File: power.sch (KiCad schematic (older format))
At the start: 20 parts, among them J4 DYN, J7 LI+, U3 LF50_TO220, U4 MCP73832-2-OT, U5 TLV75733PDBV, U6 TS881xLx

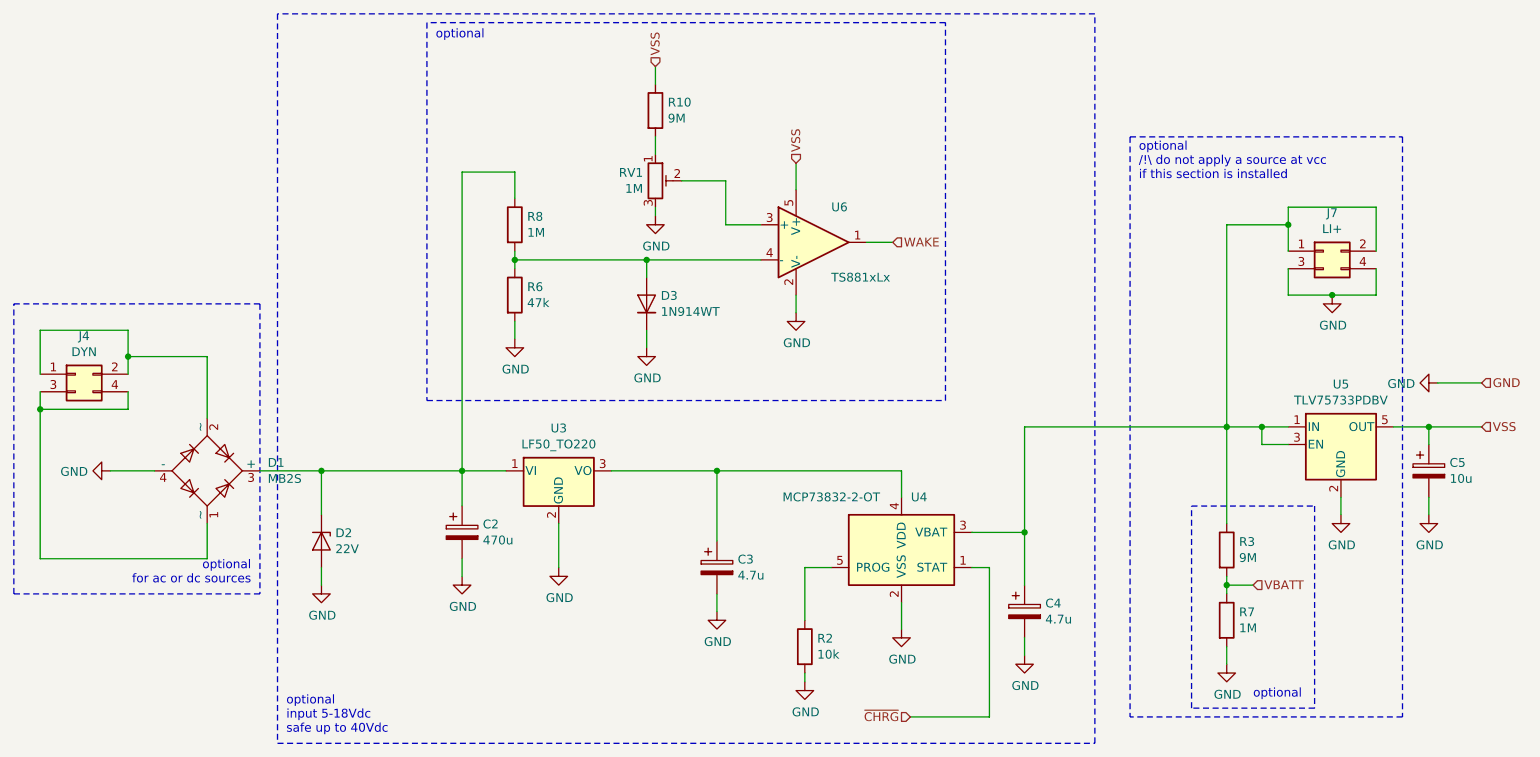
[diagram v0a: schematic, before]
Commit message: added readme and specified some field values
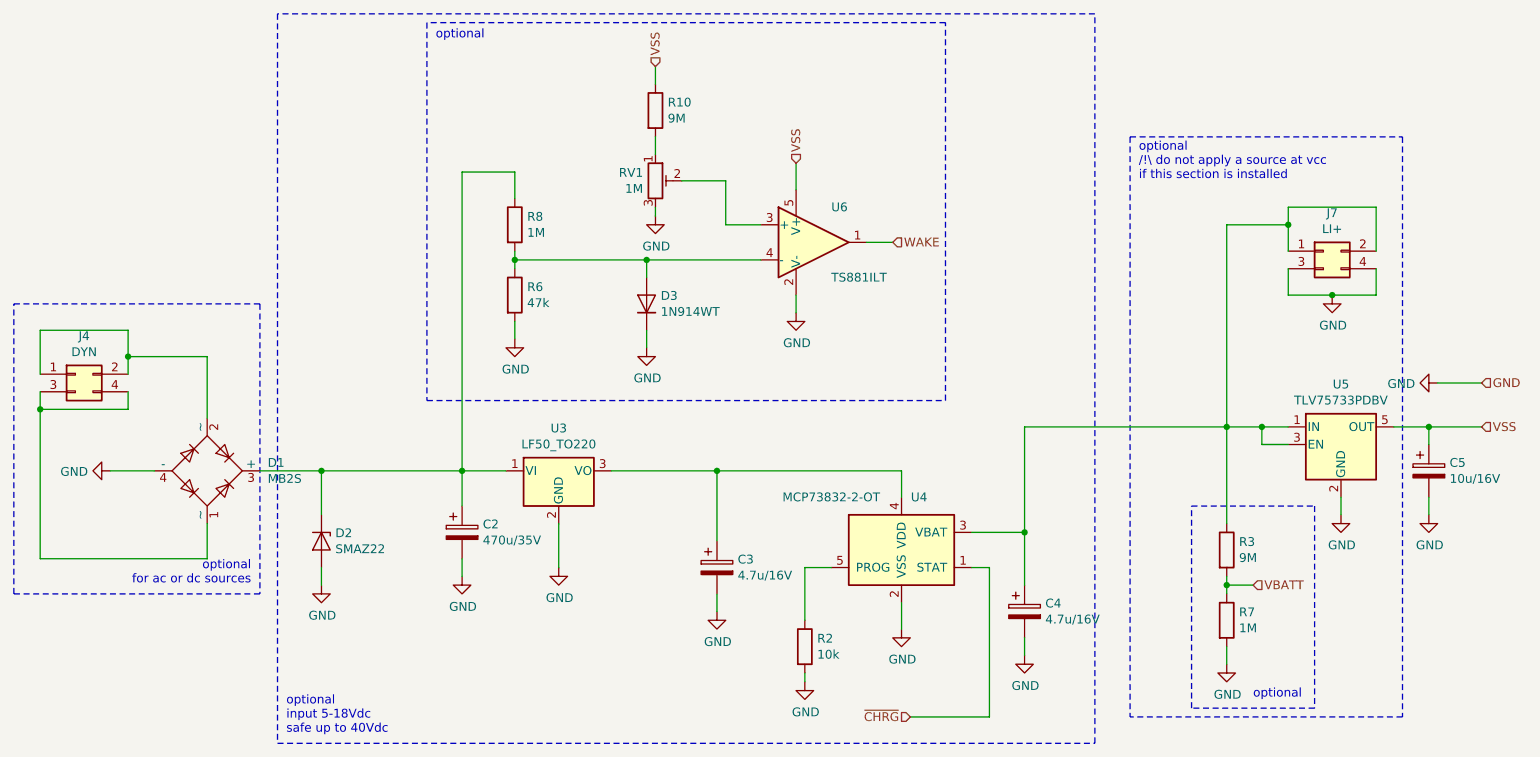
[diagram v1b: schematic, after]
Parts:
- C2: value 470u -> 470u/35V
- C3, C4: value 4.7u -> 4.7u/16V
- C5: value 10u -> 10u/16V
- D2: value 22V -> SMAZ22
- U6: value TS881xLx -> TS881ILT
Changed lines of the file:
@@
 P 6200 3050
 F 0 "U6" H 6300 3250 50  0000 L CNN
-F 1 "TS881xLx" H 6300 2850 50  0000 L CNN
+F 1 "TS881ILT" H 6300 2850 50  0000 L CNN
 F 2 "Package_TO_SOT_SMD:SOT-23-5" H 6100 2850 50  0001 L CNN
 F 3 "www.st.com/resource/en/datasheet/ts881.pdf" H 6200 3250 50  0001 C CNN
@@
 P 9700 4350
 F 0 "C5" H 9818 4396 50  0000 L CNN
-F 1 "10u" H 9818 4305 50  0000 L CNN
+F 1 "10u/16V" H 9818 4305 50  0000 L CNN
 F 2 "Capacitor_Tantalum_SMD:CP_EIA-6032-28_Kemet-C_Pad2.25x2.35mm_HandSolder" H 9738 4200 50  0001 C CNN
-F 3 "~" H 9700 4350 50  0001 C CNN
+F 3 "https://www.mouser.de/datasheet/2/212/KEM_T2005_T491-1093550.pdf" H 9700 4350 50  0001 C CNN
 	1    9700 4350
 	1    0    0    -1
@@
 P 4200 4700
 F 0 "C2" H 4318 4746 50  0000 L CNN
-F 1 "470u" H 4318 4655 50  0000 L CNN
+F 1 "470u/35V" H 4318 4655 50  0000 L CNN
 F 2 "Capacitor_THT:CP_Radial_D8.0mm_P3.50mm" H 4238 4550 50  0001 C CNN
 F 3 "https://www.mouser.de/datasheet/2/315/ABA0000C1022-1144690.pdf" H 4200 4700 50  0001 C CNN
@@
 P 7400 5150
 F 0 "C4" H 7518 5196 50  0000 L CNN
-F 1 "4.7u" H 7518 5105 50  0000 L CNN
+F 1 "4.7u/16V" H 7518 5105 50  0000 L CNN
 F 2 "Capacitor_Tantalum_SMD:CP_EIA-6032-28_Kemet-C_Pad2.25x2.35mm_HandSolder" H 7650 4150 50  0001 C CNN
-F 3 "~" H 7400 5150 50  0001 C CNN
+F 3 "https://www.mouser.de/datasheet/2/212/KEM_T2005_T491-1093550.pdf" H 7400 5150 50  0001 C CNN
 	1    7400 5150
 	1    0    0    -1
@@
 P 5650 4900
 F 0 "C3" H 5768 4946 50  0000 L CNN
-F 1 "4.7u" H 5768 4855 50  0000 L CNN
+F 1 "4.7u/16V" H 5768 4855 50  0000 L CNN
 F 2 "Capacitor_Tantalum_SMD:CP_EIA-6032-28_Kemet-C_Pad2.25x2.35mm_HandSolder" H 5688 4750 50  0001 C CNN
-F 3 "~" H 5650 4900 50  0001 C CNN
+F 3 "https://www.mouser.de/datasheet/2/212/KEM_T2005_T491-1093550.pdf" H 5650 4900 50  0001 C CNN
 	1    5650 4900
 	1    0    0    -1
@@
 P 3400 4750
 F 0 "D2" V 3354 4829 50  0000 L CNN
-F 1 "22V" V 3445 4829 50  0000 L CNN
+F 1 "SMAZ22" V 3445 4829 50  0000 L CNN
 F 2 "Diode_SMD:D_SMA_Handsoldering" H 3400 4750 50  0001 C CNN
 F 3 "https://www.mouser.de/datasheet/2/115/ds18015-38228.pdf" H 3400 4750 50  0001 C CNN
